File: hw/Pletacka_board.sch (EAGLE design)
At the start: 0 parts

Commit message: Add LEDs, RFID, Temp sen.
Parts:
- added LED1, LED2, LED3: (no value), led:LEDCHIPLED_0603
- added R1, R2, R3: (no value), rcl_upravena:R-EU_R0603
- added RDM1: RDM6300, RDM6300:RDM6300
- added U$1: ESP-32-T-DISPLAY, ESP32-T-Display:ESP-32-T-DISPLAY
- added U1: LM75BDP, LM75BDP:LM75BDP
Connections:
- new net +3V3: U$1.3V3, U1.VCC
- new net +5V: RDM1.VCC, U$1.5V5
- new net GND: LED1.C, LED2.C, LED3.C, RDM1.GND, U$1.GND, U1.GND
- new net LED_POWER: R1.1, U$1.25
- new net LED_SEND: R3.1, U$1.27
- new net LED_WIFI: R2.1, U$1.26
- new net N$1: LED1.A, R1.2
- new net N$11: U$1.33
- new net N$12: LED3.A, R3.2
- new net N$2: LED2.A, R2.2
- new net N$3: U$1.17
- new net N$4: U$1.2
- new net N$5: U$1.15
- new net N$6: U$1.13
- new net N$7: U$1.12
- new net OPTO1: U$1.36
- new net OPTO2: U$1.37
- new net OPTO3: U$1.38
- new net OPTO4: U$1.39
- new net RFID: RDM1.RX, U$1.32
- new net TMP_SCL: U$1.22, U1.SCL
- new net TMP_SDA: U$1.21, U1.SDA

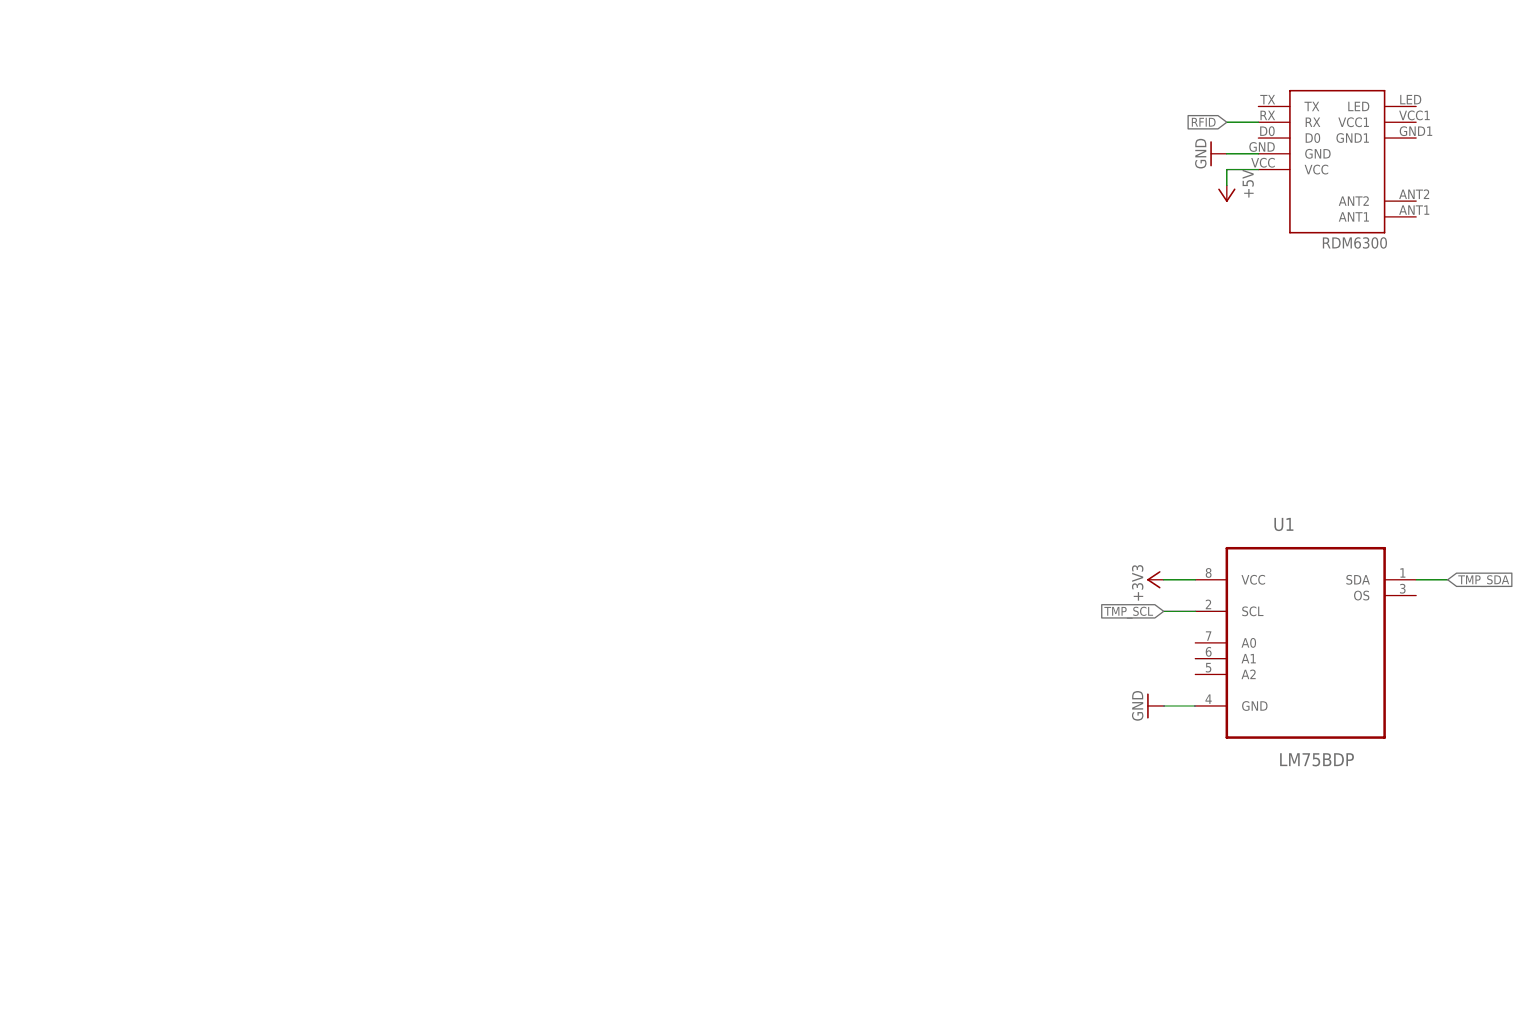
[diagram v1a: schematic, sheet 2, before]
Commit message: Add Buttons + optocouplers
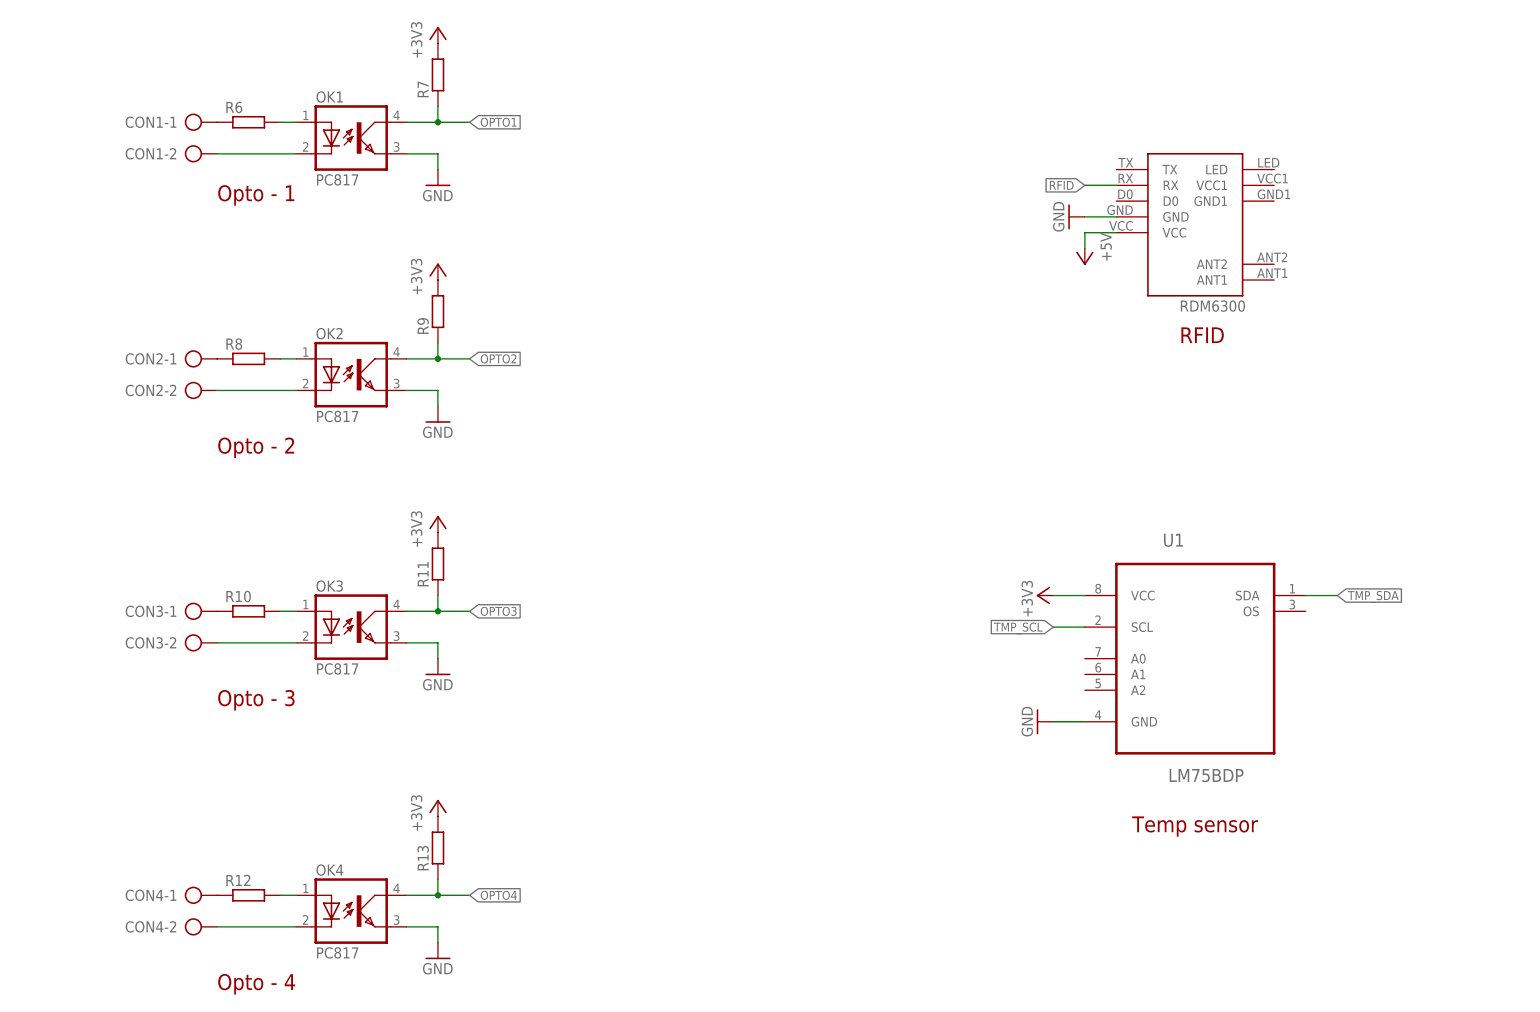
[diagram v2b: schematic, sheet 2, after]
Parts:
- added CON1, CON2, CON3, CON4: (no value), #Svorkovnice:AK500/2
- added OK1, OK2, OK3, OK4: PC817, #Optocleny:PC817
- added R10, R11, R12, R13, R6, R7, R8, R9: (no value), rcl_upravena:R-EU_R0603
- added R4, R5: 330R, rcl_upravena:R-EU_R0603
- added S1, S2: (no value), switch-omron:10-XX
- R1, R2, R3: value (none) -> 330R
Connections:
- new net BUTTON1: R4.1, U$1.13
- new net BUTTON2: R5.1, U$1.12
- new net N$10: R5.2, S2.P, S2.P1
- new net N$13: CON2-1.KL, R8.1
- new net N$14: CON2-2.KL, OK2.C
- new net N$15: OK2.A, R8.2
- new net N$16: CON3-1.KL, R10.1
- new net N$17: CON3-2.KL, OK3.C
- new net N$18: OK3.A, R10.2
- new net N$19: CON4-1.KL, R12.1
- new net N$20: CON4-2.KL, OK4.C
- new net N$21: OK4.A, R12.2
- new net N$8: R4.2, S1.P, S1.P1
- new net N$9: OK1.A, R6.2
- net +3V3: now also R11.2, R13.2, R7.2, R9.2
- net GND: now also OK1.EMIT, OK2.EMIT, OK3.EMIT, OK4.EMIT, S1.S, S1.S1, S2.S, S2.S1
- net N$6: now also CON1-1.KL, R6.1; no longer U$1.13
- net N$7: now also CON1-2.KL, OK1.C; no longer U$1.12
- net OPTO1: now also OK1.COL, R7.1
- net OPTO2: now also OK2.COL, R9.1
- net OPTO3: now also OK3.COL, R11.1
- net OPTO4: now also OK4.COL, R13.1
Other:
- note added: "Opto - 1"
- note added: "Opto - 2"
- note added: "Opto - 3"
- note added: "Opto - 4"
- note added: "RFID"
- note added: "Temp sensor"
- moved on the sheet: LED1, LED2, LED3, R1, R2, R3, U$1, U1

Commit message: Start power management
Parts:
- removed OK1, OK2, OK3, OK4: PC817, #Optocleny:PC817
- added C1: 10u, rcl_upravena:C-EUC0402
- added C10: 22u, rcl_upravena:C-EUC0402
- added C11: 100n, rcl_upravena:C-EUC0402
- added C12: 8.2n, rcl_upravena:C-EUC0402
- added C2: 10p, rcl_upravena:C-EUC0402
- added C3: 6.8n, rcl_upravena:C-EUC0402
- added CON5: (no value), #Svorkovnice:AK500/2
- added R14: 169K, rcl:R-EU_R0402
- added R15: 16.2k, rcl:R-EU_R0402
- added R16: 8.25k, rcl:R-EU_R0402
- added R22: 1.69k, rcl:R-EU_R0402
- added R23: 10.2k, rcl:R-EU_R0402
- added U2, U3, U4, U5: EL357N(A)(TA)-G, EL357N_A__TA_-G:EL357N(A)(TA)-G
- added U6: TPS54231D, TPS54231D:TPS54231D
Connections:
- new net N$22: C1.1, CON5-1.KL, R14.2, U6.VIN
- new net N$23: R14.1, R15.2, U6.EN
- new net N$25: C3.1, R16.1
- new net N$26: C2.1, R16.2, U6.COMP
- new net N$34: R22.2, R23.1, U6.VSENSE
- new net N$35: C11.1, U6.BOOT
- new net N$36: C11.2, U6.PH
- new net N$37: C12.1, U6.SS
- net +5V: now also C10.1, R23.2
- net GND: now also C1.2, C10.2, C12.2, C2.2, C3.2, CON5-2.KL, R15.1, R22.1, U2.E, U3.E, U4.E, U5.E, U6.GND; no longer OK1.EMIT, OK2.EMIT, OK3.EMIT, OK4.EMIT
- net N$14: now also U3.K; no longer OK2.C
- net N$15: now also U3.A; no longer OK2.A
- net N$17: now also U4.K; no longer OK3.C
- net N$18: now also U4.A; no longer OK3.A
- net N$20: now also U5.K; no longer OK4.C
- net N$21: now also U5.A; no longer OK4.A
- net N$7: now also U2.K; no longer OK1.C
- net N$9: now also U2.A; no longer OK1.A
- net OPTO1: now also U2.C; no longer OK1.COL
- net OPTO2: now also U3.C; no longer OK2.COL
- net OPTO3: now also U4.C; no longer OK3.COL
- net OPTO4: now also U5.C; no longer OK4.COL
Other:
- note added: "47uH, 94mOhm"
- note added: "550mV, 1A"
- note added: "Cívka"
- note added: "Dioda"
- note added: "Input - 24V"
- note added: "Neni basic"

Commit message: cesgaw
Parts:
- added C4, C5: 1u, rcl_upravena:C-EUC0603
- added D1: B5819W, B5819W:B5819W
- C1: LSCS_ID (none) -> C19702
- C10: LCSC_ID (none) -> C59461
- C11: LCSC_ID (none) -> C14663
- C12: LCSC_ID (none) -> C27920
- C2: LCSC_ID (none) -> C1634
- C3: LCSC_ID (none) -> C1631
- R1, R2, R3, R4, R5: value 330R -> 2k2
- R11, R13, R7, R9: value (none) -> 10k
- R14: value 169K -> 160k; LCSC_ID (none) -> C22813
- R15: value 16.2k -> 16k; LSCS_ID (none) -> C22818
- R16: value 8.25k -> 8.2k; LCSC_ID (none) -> C25981
- R22: value 1.69k -> 1.8k; LCSC_ID (none) -> C4177
- R23: value 10.2k -> 10k; LCSC_ID (none) -> C25804
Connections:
- net GND: now also C4.1, C5.1, D1.A
- net N$10: now also C4.2
- net N$36: now also D1.C
- net N$8: now also C5.2
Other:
- note added: "Z rbc"
- note removed: "550mV, 1A"
- note removed: "Dioda"
- note removed: "Neni basic"
- moved on the sheet: R4, R5

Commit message: Start routing
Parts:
- removed RDM1: RDM6300, RDM6300:RDM6300
- added U$2: SWRB1204S, SWRB1204S-680MT:SWRB1204S
- C1, C10, C11, C12, C2, C3: device rcl_upravena:C-EUC0402 -> rcl_upravena:C-EUC0603
- C5: LCSC_ID (none) -> C15849
- D1: LSCS_ID (none) -> C8598
- LED1, LED2, LED3: LCSC_ID (none) -> C2286
- R1, R2, R3, R4, R5: LCSC_ID (none) -> C4190
- R10, R12, R6, R8: value (none) -> 1k; LSCS_ID (none) -> C21190
- R11, R13, R7, R9: LSCS_ID (none) -> C25804
- R14, R15, R16, R22, R23: device rcl:R-EU_R0402 -> rcl_upravena:R-EU_R0603
- S1, S2: value (none) -> CHOOSE_ME; device switch-omron:10-XX -> switch-omron:10-XX_SMD
- U1: LCSC_ID (none) -> C33099
- U2: LSCS_ID (none) -> C6649
- U3, U4, U5: LCSC_ID (none) -> C6649
- U6: LCSC_ID (none) -> C28023
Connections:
- net N$22 renamed VIN
- net N$23 renamed EN
- net N$26 renamed COMP
- net N$34 renamed VSENSE
- net N$35 renamed BOOT
- net N$37 renamed SS
- removed net N$11: U$1.33
- removed net N$36: C11.2, D1.C, U6.PH
- new net PH: C11.2, D1.C, U$2.P$1, U6.PH
- new net TMP_OS: U$1.33, U1.OS
- net +5V: now also U$2.P$2; no longer RDM1.VCC
- net GND: now also S1.P, S1.P1, S2.P, S2.P1, U1.A0, U1.A1, U1.A2; no longer RDM1.GND, S1.S, S1.S1, S2.S, S2.S1
- net N$10: now also S2.S, S2.S1; no longer S2.P, S2.P1
- net N$8: now also S1.S, S1.S1; no longer S1.P, S1.P1
- net RFID: no longer RDM1.RX
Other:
- note added: "Addr: 0b1001000 (72)"
- note removed: "47uH, 94mOhm"
- note removed: "Cívka"
- note removed: "RFID"
- note removed: "Z rbc"
- moved on the sheet: C11, C4, C5, R5, S2

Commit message: Finish first routing
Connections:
- net RFID renamed N$3
- removed net N$3 (its old number): U$1.17
- new net N$27: U$1.13
- net BUTTON1: now also U$1.21; no longer U$1.13
- net N$4: now also U$1.33; no longer U$1.2
- net TMP_OS: now also U$1.2; no longer U$1.33
- net TMP_SCL: now also U$1.17; no longer U$1.22
- net TMP_SDA: now also U$1.22; no longer U$1.21
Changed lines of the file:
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@@
-</segment>
-</net>
-<net name="TMP_SDA" class="0">
-<segment>
-<pinref part="U$1" gate="G$1" pin="21"/>
-<wire x1="48.26" y1="106.68" x2="43.18" y2="106.68" width="0.1524" layer="91"/>
-<label x="43.18" y="106.68" size="1.27" layer="95" rot="R180" xref="yes"/>
-</segment>
-</net>
-<net name="TMP_SCL" class="0">
-<segment>
-<pinref part="U$1" gate="G$1" pin="22"/>
-<wire x1="48.26" y1="104.14" x2="43.18" y2="104.14" width="0.1524" layer="91"/>
-<label x="43.18" y="104.14" size="1.27" layer="95" rot="R180" xref="yes"/>
-</segment>
-</net>
-<net name="N$3" class="0">
-<segment>
-<pinref part="U$1" gate="G$1" pin="17"/>
-<wire x1="48.26" y1="101.6" x2="43.18" y2="101.6" width="0.1524" layer="91"/>
-</segment>
-</net>
-<net name="N$4" class="0">
-<segment>
-<pinref part="U$1" gate="G$1" pin="2"/>
-<wire x1="48.26" y1="99.06" x2="43.18" y2="99.06" width="0.1524" layer="91"/>
-</segment>
-</net>
-<net name="N$5" class="0">
-<segment>
-<pinref part="U$1" gate="G$1" pin="15"/>
-<wire x1="48.26" y1="96.52" x2="43.18" y2="96.52" width="0.1524" layer="91"/>
-</segment>
-</net>
-<net name="TMP_OS" class="0">
-<segment>
-<pinref part="U$1" gate="G$1" pin="33"/>
-<wire x1="83.82" y1="96.52" x2="88.9" y2="96.52" width="0.1524" layer="91"/>
-<label x="88.9" y="96.52" size="1.27" layer="95" xref="yes"/>
-</segment>
-</net>
-<net name="RFID" class="0">
-<segment>
-<pinref part="U$1" gate="G$1" pin="32"/>
-<wire x1="83.82" y1="99.06" x2="88.9" y2="99.06" width="0.1524" layer="91"/>
 </segment>
 </net>
@@
 </segment>
 <segment>
-<pinref part="U$1" gate="G$1" pin="13"/>
-<wire x1="48.26" y1="93.98" x2="43.18" y2="93.98" width="0.1524" layer="91"/>
-<label x="43.18" y="93.98" size="1.27" layer="95" rot="R180" xref="yes"/>
+<pinref part="U$1" gate="G$1" pin="21"/>
+<wire x1="48.26" y1="106.68" x2="43.18" y2="106.68" width="0.1524" layer="91"/>
+<label x="43.18" y="106.68" size="1.27" layer="95" rot="R180" xref="yes"/>
 </segment>
 </net>
@@
 <wire x1="48.26" y1="91.44" x2="43.18" y2="91.44" width="0.1524" layer="91"/>
 <label x="43.18" y="91.44" size="1.27" layer="95" rot="R180" xref="yes"/>
+</segment>
+</net>
+<net name="TMP_SDA" class="0">
+<segment>
+<pinref part="U$1" gate="G$1" pin="22"/>
+<wire x1="48.26" y1="104.14" x2="43.18" y2="104.14" width="0.1524" layer="91"/>
+<label x="43.18" y="104.14" size="1.27" layer="95" rot="R180" xref="yes"/>
+</segment>
+</net>
+<net name="TMP_SCL" class="0">
+<segment>
+<pinref part="U$1" gate="G$1" pin="17"/>
+<wire x1="48.26" y1="101.6" x2="43.18" y2="101.6" width="0.1524" layer="91"/>
+<label x="43.18" y="101.6" size="1.27" layer="95" rot="R180" xref="yes"/>
+</segment>
+</net>
+<net name="TMP_OS" class="0">
+<segment>
+<pinref part="U$1" gate="G$1" pin="2"/>
+<wire x1="48.26" y1="99.06" x2="43.18" y2="99.06" width="0.1524" layer="91"/>
+<label x="43.18" y="99.06" size="1.27" layer="95" rot="R180" xref="yes"/>
+</segment>
+</net>
+<net name="N$26" class="0">
+<segment>
+<pinref part="U$1" gate="G$1" pin="15"/>
+<wire x1="48.26" y1="96.52" x2="43.18" y2="96.52" width="0.1524" layer="91"/>
+</segment>
+</net>
+<net name="N$27" class="0">
+<segment>
+<pinref part="U$1" gate="G$1" pin="13"/>
+<wire x1="48.26" y1="93.98" x2="43.18" y2="93.98" width="0.1524" layer="91"/>
+</segment>
+</net>
+<net name="N$3" class="0">
+<segment>
+<pinref part="U$1" gate="G$1" pin="32"/>
+<wire x1="83.82" y1="99.06" x2="88.9" y2="99.06" width="0.1524" layer="91"/>
+</segment>
+</net>
+<net name="N$4" class="0">
+<segment>
+<pinref part="U$1" gate="G$1" pin="33"/>
+<wire x1="83.82" y1="96.52" x2="88.9" y2="96.52" width="0.1524" layer="91"/>
 </segment>
 </net>
@@
 </sheet>
 </sheets>
+<errors>
+</errors>
 </schematic>
 </drawing>

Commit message: Add 2 pinheads
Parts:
- added JP1: (no value), pinhead:PINHD-1X3
- added JP2: (no value), pinhead:PINHD-1X4
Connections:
- removed net N$26: U$1.15
- removed net N$27: U$1.13
- removed net N$3: U$1.32
- removed net N$4: U$1.33
- new net GPIO13: JP2.3, U$1.13
- new net GPIO15: JP2.4, U$1.15
- new net GPIO32: JP2.1, U$1.32
- new net GPIO33: JP2.2, U$1.33
- net +3V3: now also JP1.2
- net +5V: now also JP1.3
- net GND: now also JP1.1
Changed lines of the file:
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@@
 <part name="S1" library="switch-omron" deviceset="10-XX" device="_SMD" value="CHOOSE_ME"/>
 <part name="S2" library="switch-omron" deviceset="10-XX" device="_SMD" value="CHOOSE_ME"/>
+<part name="GND2" library="supply1" library_urn="urn:adsk.eagle:library:371" deviceset="GND" device=""/>
+<part name="+3V7" library="supply1" library_urn="urn:adsk.eagle:library:371" deviceset="+3V3" device=""/>
+<part name="P+2" library="supply1" library_urn="urn:adsk.eagle:library:371" deviceset="+5V" device=""/>
+<part name="JP1" library="pinhead" library_urn="urn:adsk.eagle:library:325" deviceset="PINHD-1X3" device="" package3d_urn="urn:adsk.eagle:package:22458/2"/>
+<part name="JP2" library="pinhead" library_urn="urn:adsk.eagle:library:325" deviceset="PINHD-1X4" device="" package3d_urn="urn:adsk.eagle:package:22407/2"/>
 </parts>
 <sheets>
@@
 <instance part="S2" gate="1" x="208.28" y="60.96" smashed="yes" rot="MR270">
 <attribute name="NAME" x="208.28" y="66.04" size="1.27" layer="95" rot="R180" align="top-center"/>
+</instance>
+<instance part="GND2" gate="1" x="96.52" y="43.18" smashed="yes" rot="R270">
+<attribute name="VALUE" x="93.98" y="45.72" size="1.778" layer="96" rot="R270"/>
+</instance>
+<instance part="+3V7" gate="G$1" x="86.36" y="40.64" smashed="yes" rot="R90">
+<attribute name="VALUE" x="91.44" y="38.1" size="1.778" layer="96" rot="R180"/>
+</instance>
+<instance part="P+2" gate="1" x="101.6" y="38.1" smashed="yes" rot="R90">
+<attribute name="VALUE" x="104.394" y="41.402" size="1.778" layer="96" rot="R180"/>
+</instance>
+<instance part="JP1" gate="A" x="116.84" y="40.64" smashed="yes">
+<attribute name="NAME" x="110.49" y="46.355" size="1.778" layer="95"/>
+<attribute name="VALUE" x="110.49" y="33.02" size="1.778" layer="96"/>
+</instance>
+<instance part="JP2" gate="A" x="116.84" y="17.78" smashed="yes">
+<attribute name="NAME" x="110.49" y="26.035" size="1.778" layer="95"/>
+<attribute name="VALUE" x="110.49" y="10.16" size="1.778" layer="96"/>
 </instance>
 </instances>
@@
 <pinref part="S1" gate="1" pin="P1"/>
 </segment>
+<segment>
+<wire x1="114.3" y1="43.18" x2="99.06" y2="43.18" width="0.1524" layer="91"/>
+<pinref part="GND2" gate="1" pin="GND"/>
+<pinref part="JP1" gate="A" pin="1"/>
+</segment>
 </net>
 <net name="+3V3" class="0">
@@
 <wire x1="43.18" y1="83.82" x2="48.26" y2="83.82" width="0.1524" layer="91"/>
 </segment>
+<segment>
+<wire x1="114.3" y1="40.64" x2="88.9" y2="40.64" width="0.1524" layer="91"/>
+<pinref part="+3V7" gate="G$1" pin="+3V3"/>
+<pinref part="JP1" gate="A" pin="2"/>
+</segment>
 </net>
 <net name="+5V" class="0">
@@
 <pinref part="P+1" gate="1" pin="+5V"/>
 <wire x1="83.82" y1="83.82" x2="88.9" y2="83.82" width="0.1524" layer="91"/>
+</segment>
+<segment>
+<wire x1="114.3" y1="38.1" x2="104.14" y2="38.1" width="0.1524" layer="91"/>
+<pinref part="P+2" gate="1" pin="+5V"/>
+<pinref part="JP1" gate="A" pin="3"/>
 </segment>
 </net>
@@
 </segment>
 </net>
-<net name="N$26" class="0">
+<net name="GPIO15" class="0">
 <segment>
 <pinref part="U$1" gate="G$1" pin="15"/>
 <wire x1="48.26" y1="96.52" x2="43.18" y2="96.52" width="0.1524" layer="91"/>
-</segment>
-</net>
-<net name="N$27" class="0">
+<label x="43.18" y="96.52" size="1.27" layer="95" rot="R180" xref="yes"/>
+</segment>
+<segment>
+<pinref part="JP2" gate="A" pin="4"/>
+<wire x1="114.3" y1="15.24" x2="106.68" y2="15.24" width="0.1524" layer="91"/>
+<label x="106.68" y="15.24" size="1.27" layer="95" rot="R180" xref="yes"/>
+</segment>
+</net>
+<net name="GPIO13" class="0">
 <segment>
 <pinref part="U$1" gate="G$1" pin="13"/>
 <wire x1="48.26" y1="93.98" x2="43.18" y2="93.98" width="0.1524" layer="91"/>
-</segment>
-</net>
-<net name="N$3" class="0">
+<label x="43.18" y="93.98" size="1.27" layer="95" rot="R180" xref="yes"/>
+</segment>
+<segment>
+<pinref part="JP2" gate="A" pin="3"/>
+<wire x1="114.3" y1="17.78" x2="106.68" y2="17.78" width="0.1524" layer="91"/>
+<label x="106.68" y="17.78" size="1.27" layer="95" rot="R180" xref="yes"/>
+</segment>
+</net>
+<net name="GPIO32" class="0">
 <segment>
 <pinref part="U$1" gate="G$1" pin="32"/>
 <wire x1="83.82" y1="99.06" x2="88.9" y2="99.06" width="0.1524" layer="91"/>
-</segment>
-</net>
-<net name="N$4" class="0">
+<label x="88.9" y="99.06" size="1.27" layer="95" xref="yes"/>
+</segment>
+<segment>
+<pinref part="JP2" gate="A" pin="1"/>
+<wire x1="114.3" y1="22.86" x2="106.68" y2="22.86" width="0.1524" layer="91"/>
+<label x="106.68" y="22.86" size="1.27" layer="95" rot="R180" xref="yes"/>
+</segment>
+</net>
+<net name="GPIO33" class="0">
 <segment>
 <pinref part="U$1" gate="G$1" pin="33"/>
 <wire x1="83.82" y1="96.52" x2="88.9" y2="96.52" width="0.1524" layer="91"/>
-</segment>
-</net>
+<label x="88.9" y="96.52" size="1.27" layer="95" xref="yes"/>
+</segment>
+<segment>
+<pinref part="JP2" gate="A" pin="2"/>
+<wire x1="114.3" y1="20.32" x2="106.68" y2="20.32" width="0.1524" layer="91"/>
+<label x="106.68" y="20.32" size="1.27" layer="95" rot="R180" xref="yes"/>
+</segment>
+</net>
